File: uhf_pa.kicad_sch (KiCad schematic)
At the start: 24 parts, among them U12 FPF2701, U13 TQP7M9106

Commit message: Add manufacture number and JLCPCB part number to components
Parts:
- C67: JLCPCB Part # (none) -> C88885; Manufacturer_Part_Number (none) -> GJM1555C1H2R0WB01D
- C68: JLCPCB Part # (none) -> C2168987; Manufacturer_Part_Number (none) -> CGA2B3X5R1H104K050BB
- C70, C75, C76: JLCPCB Part # (none) -> C386123; Manufacturer_Part_Number (none) -> UMK105CG101JV-F
- C71: JLCPCB Part # (none) -> C2182156; Manufacturer_Part_Number (none) -> EMK212BB7106KG-T
- C72: JLCPCB Part # (none) -> C1711; Manufacturer_Part_Number (none) -> CL21B104KBCNNNC
- C73: JLCPCB Part # (none) -> C1959557; Manufacturer_Part_Number (none) -> T495C106K035ATE400
- C74: JLCPCB Part # (none) -> C2195556; Manufacturer_Part_Number (none) -> C0402C102K5GECAUTO7411
- C77: JLCPCB Part # (none) -> C3833393; Manufacturer_Part_Number (none) -> UMK105CG240JV-F
- C78: JLCPCB Part # (none) -> C88892; Manufacturer_Part_Number (none) -> GJM1555C1H3R3WB01D
- FB1: JLCPCB Part # (none) -> C85832; Manufacturer_Part_Number (none) -> BLM18KG331SN1D
- L14: JLCPCB Part # (none) -> C2043867; Manufacturer_Part_Number (none) -> LQW15AN4N0B8ZD
- L16: JLCPCB Part # (none) -> C2049784; Manufacturer_Part_Number (none) -> LQW15AN68NJ0ZD
- L17: JLCPCB Part # (none) -> C344018; Manufacturer_Part_Number (none) -> LQW15AN18NJ80D
- L18: JLCPCB Part # (none) -> C341788; Manufacturer_Part_Number (none) -> LQW15AN8N2H00D
- L19: JLCPCB Part # (none) -> C3222081; Manufacturer_Part_Number (none) -> LQW15AN47NJ8ZD
- R27: JLCPCB Part # (none) -> C843898; Manufacturer_Part_Number (none) -> CRCW0402240RFKEDC
- R28: JLCPCB Part # (none) -> C273692; Manufacturer_Part_Number (none) -> RC0402FR-07280RL
- R30, R31: JLCPCB Part # (none) -> C4176290; Manufacturer_Part_Number (none) -> ERJ-H3EF1103V
- U12: JLCPCB Part # (none) -> C891252; Manufacturer_Part_Number (none) -> FPF2701MPX
- U13: JLCPCB Part # (none) -> C920265; Manufacturer_Part_Number (none) -> TQP7M9106
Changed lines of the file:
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@@
+      (effects (font (size 1.27 1.27)) hide)
+    )
+    (property "JLCPCB Part #" "C344018" (id 5) (at 175.26 123.19 0)
+      (effects (font (size 1.27 1.27)) hide)
+    )
+    (property "Manufacturer_Part_Number" "LQW15AN18NJ80D " (id 6) (at 175.26 123.19 0)
       (effects (font (size 1.27 1.27)) hide)
     )
@@
     )
     (property "PartNumber" "LQW15AN47NJ8ZD" (id 4) (at 201.93 127 0)
+      (effects (font (size 1.27 1.27)) hide)
+    )
+    (property "JLCPCB Part #" "C3222081" (id 5) (at 201.93 127 0)
+      (effects (font (size 1.27 1.27)) hide)
+    )
+    (property "Manufacturer_Part_Number" "LQW15AN47NJ8ZD " (id 6) (at 201.93 127 0)
       (effects (font (size 1.27 1.27)) hide)
     )
@@
     )
     (property "PartNumber" "EMK212BB7106KG-T" (id 6) (at 144.78 33.02 0)
+      (effects (font (size 1.27 1.27)) hide)
+    )
+    (property "JLCPCB Part #" "C2182156" (id 7) (at 144.78 33.02 0)
+      (effects (font (size 1.27 1.27)) hide)
+    )
+    (property "Manufacturer_Part_Number" "EMK212BB7106KG-T" (id 8) (at 144.78 33.02 0)
       (effects (font (size 1.27 1.27)) hide)
     )
@@
       (effects (font (size 1.27 1.27)) hide)
     )
+    (property "JLCPCB Part #" "C2168987" (id 7) (at 100.33 106.68 0)
+      (effects (font (size 1.27 1.27)) hide)
+    )
+    (property "Manufacturer_Part_Number" "CGA2B3X5R1H104K050BB " (id 8) (at 100.33 106.68 0)
+      (effects (font (size 1.27 1.27)) hide)
+    )
     (pin "1")
     (pin "2")
@@
     )
     (property "PartNumber" "FPF2701MPX" (id 5) (at 139.7 49.53 0)
+      (effects (font (size 1.27 1.27)) hide)
+    )
+    (property "Manufacturer_Part_Number" "FPF2701MPX " (id 6) (at 139.7 49.53 0)
+      (effects (font (size 1.27 1.27)) hide)
+    )
+    (property "JLCPCB Part #" "C891252" (id 7) (at 139.7 49.53 0)
       (effects (font (size 1.27 1.27)) hide)
     )
@@
       (effects (font (size 1.27 1.27)) hide)
     )
+    (property "JLCPCB Part #" "C2049784" (id 7) (at 107.95 111.76 0)
+      (effects (font (size 1.27 1.27)) hide)
+    )
+    (property "Manufacturer_Part_Number" "LQW15AN68NJ0ZD " (id 8) (at 107.95 111.76 0)
+      (effects (font (size 1.27 1.27)) hide)
+    )
     (pin "1")
     (pin "2")
@@
       (effects (font (size 1.27 1.27)) hide)
     )
+    (property "JLCPCB Part #" "C2195556" (id 7) (at 180.34 101.6 0)
+      (effects (font (size 1.27 1.27)) hide)
+    )
+    (property "Manufacturer_Part_Number" "C0402C102K5GECAUTO7411 " (id 8) (at 180.34 101.6 0)
+      (effects (font (size 1.27 1.27)) hide)
+    )
     (pin "1")
     (pin "2")
@@
     )
     (property "PartNumber" "" (id 6) (at 115.57 96.52 0)
+      (effects (font (size 1.27 1.27)) hide)
+    )
+    (property "JLCPCB Part #" "C273692" (id 7) (at 115.57 96.52 0)
+      (effects (font (size 1.27 1.27)) hide)
+    )
+    (property "Manufacturer_Part_Number" "RC0402FR-07280RL " (id 8) (at 115.57 96.52 0)
       (effects (font (size 1.27 1.27)) hide)
     )
@@
       (effects (font (size 1.27 1.27)) hide)
     )
+    (property "JLCPCB Part #" "C3833393" (id 6) (at 189.23 127 0)
+      (effects (font (size 1.27 1.27)) hide)
+    )
+    (property "Manufacturer_Part_Number" "UMK105CG240JV-F" (id 7) (at 189.23 127 0)
+      (effects (font (size 1.27 1.27)) hide)
+    )
     (pin "1")
     (pin "2")
@@
       (effects (font (size 1.27 1.27)) hide)
     )
+    (property "JLCPCB Part #" "C386123" (id 7) (at 180.34 119.38 0)
+      (effects (font (size 1.27 1.27)) hide)
+    )
+    (property "Manufacturer_Part_Number" "UMK105CG101JV-F" (id 8) (at 180.34 119.38 0)
+      (effects (font (size 1.27 1.27)) hide)
+    )
     (pin "1")
     (pin "2")
@@
     )
     (property "PartNumber" "" (id 6) (at 107.95 96.52 0)
+      (effects (font (size 1.27 1.27)) hide)
+    )
+    (property "JLCPCB Part #" "C843898" (id 7) (at 107.95 96.52 0)
+      (effects (font (size 1.27 1.27)) hide)
+    )
+    (property "Manufacturer_Part_Number" "CRCW0402240RFKEDC " (id 8) (at 107.95 96.52 0)
       (effects (font (size 1.27 1.27)) hide)
     )
@@
     )
     (property "PartNumber" "" (id 6) (at 116.84 46.99 0)
+      (effects (font (size 1.27 1.27)) hide)
+    )
+    (property "JLCPCB Part #" "C4176290" (id 7) (at 116.84 46.99 0)
+      (effects (font (size 1.27 1.27)) hide)
+    )
+    (property "Manufacturer_Part_Number" "ERJ-H3EF1103V" (id 8) (at 116.84 46.99 0)
       (effects (font (size 1.27 1.27)) hide)
     )
@@
       (effects (font (size 1.27 1.27)) hide)
     )
+    (property "JLCPCB Part #" "C386123" (id 7) (at 180.34 110.49 0)
+      (effects (font (size 1.27 1.27)) hide)
+    )
+    (property "Manufacturer_Part_Number" "UMK105CG101JV-F" (id 8) (at 180.34 110.49 0)
+      (effects (font (size 1.27 1.27)) hide)
+    )
     (pin "1")
     (pin "2")
@@
       (effects (font (size 1.27 1.27)) hide)
     )
+    (property "JLCPCB Part #" "C1959557" (id 7) (at 180.34 92.71 0)
+      (effects (font (size 1.27 1.27)) hide)
+    )
+    (property "Manufacturer_Part_Number" "T495C106K035ATE400 " (id 8) (at 180.34 92.71 0)
+      (effects (font (size 1.27 1.27)) hide)
+    )
     (pin "1")
     (pin "2")
@@
       (effects (font (size 1.27 1.27)) hide)
     )
+    (property "JLCPCB Part #" "C4176290" (id 7) (at 127 59.69 0)
+      (effects (font (size 1.27 1.27)) hide)
+    )
+    (property "Manufacturer_Part_Number" "ERJ-H3EF1103V" (id 8) (at 127 59.69 0)
+      (effects (font (size 1.27 1.27)) hide)
+    )
     (pin "1")
     (pin "2")
@@
       (effects (font (size 1.27 1.27)) hide)
     )
+    (property "JLCPCB Part #" "C1711" (id 7) (at 160.02 33.02 0)
+      (effects (font (size 1.27 1.27)) hide)
+    )
+    (property "Manufacturer_Part_Number" "CL21B104KBCNNNC " (id 8) (at 160.02 33.02 0)
+      (effects (font (size 1.27 1.27)) hide)
+    )
     (pin "1")
     (pin "2")
@@
     )
     (property "PartNumber" "LQW15AN6N0B80D" (id 4) (at 119.38 133.35 0)
+      (effects (font (size 1.27 1.27)) hide)
+    )
+    (property "JLCPCB Part #" "C2043867" (id 5) (at 119.38 133.35 0)
+      (effects (font (size 1.27 1.27)) hide)
+    )
+    (property "Manufacturer_Part_Number" "LQW15AN4N0B8ZD " (id 6) (at 119.38 133.35 0)
       (effects (font (size 1.27 1.27)) hide)
     )
@@
       (effects (font (size 1.27 1.27)) hide)
     )
+    (property "JLCPCB Part #" "C88892" (id 6) (at 214.63 127 0)
+      (effects (font (size 1.27 1.27)) hide)
+    )
+    (property "Manufacturer_Part_Number" "GJM1555C1H3R3WB01D " (id 7) (at 214.63 127 0)
+      (effects (font (size 1.27 1.27)) hide)
+    )
     (pin "1")
     (pin "2")
@@
     )
     (property "PartNumber" "LQW15AN8N2H00D" (id 4) (at 195.58 132.08 0)
+      (effects (font (size 1.27 1.27)) hide)
+    )
+    (property "JLCPCB Part #" "C341788" (id 5) (at 195.58 132.08 0)
+      (effects (font (size 1.27 1.27)) hide)
+    )
+    (property "Manufacturer_Part_Number" "LQW15AN8N2H00D " (id 6) (at 195.58 132.08 0)
       (effects (font (size 1.27 1.27)) hide)
     )
@@
       (effects (font (size 1.27 1.27)) hide)
     )
+    (property "JLCPCB Part #" "C386123" (id 7) (at 121.92 106.68 0)
+      (effects (font (size 1.27 1.27)) hide)
+    )
+    (property "Manufacturer_Part_Number" "UMK105CG101JV-F" (id 8) (at 121.92 106.68 0)
+      (effects (font (size 1.27 1.27)) hide)
+    )
     (pin "1")
     (pin "2")
@@
       (effects (font (size 1.27 1.27)) (justify right) hide)
     )
+    (property "JLCPCB Part #" "C85832" (id 6) (at 175.26 114.3 0)
+      (effects (font (size 1.27 1.27)) hide)
+    )
+    (property "Manufacturer_Part_Number" "BLM18KG331SN1D " (id 7) (at 175.26 114.3 0)
+      (effects (font (size 1.27 1.27)) hide)
+    )
     (pin "1")
     (pin "2")
@@
     )
     (property "PartNumber" "GJM1555C1H2R0WB01D" (id 5) (at 127 128.27 0)
+      (effects (font (size 1.27 1.27)) hide)
+    )
+    (property "JLCPCB Part #" "C88885" (id 6) (at 127 128.27 0)
+      (effects (font (size 1.27 1.27)) hide)
+    )
+    (property "Manufacturer_Part_Number" "GJM1555C1H2R0WB01D " (id 7) (at 127 128.27 0)
       (effects (font (size 1.27 1.27)) hide)
     )
@@
       (effects (font (size 1.27 1.27)) hide)
     )
+    (property "Manufacturer_Part_Number" "TQP7M9106 " (id 6) (at 151.13 127 0)
+      (effects (font (size 1.27 1.27)) hide)
+    )
+    (property "JLCPCB Part #" "C920265" (id 7) (at 151.13 127 0)
+      (effects (font (size 1.27 1.27)) hide)
+    )

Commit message: Update C67 part number
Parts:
- C67: JLCPCB Part # C88885 -> C576707; Manufacturer_Part_Number GJM1555C1H2R0WB01D -> CC0402JRNPO9BN500; Mnf. Murata Electronics -> (none); PartNumber GJM1555C1H2R0WB01D -> CC0402JRNPO9BN500
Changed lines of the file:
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@@
       (effects (font (size 1.27 1.27)) hide)
     )
-    (property "Mnf." "Murata Electronics" (id 4) (at 127 128.27 0)
+    (property "PartNumber" "CC0402JRNPO9BN500 " (id 5) (at 127 128.27 0)
       (effects (font (size 1.27 1.27)) hide)
     )
-    (property "PartNumber" "GJM1555C1H2R0WB01D" (id 5) (at 127 128.27 0)
+    (property "JLCPCB Part #" "C576707" (id 6) (at 127 128.27 0)
       (effects (font (size 1.27 1.27)) hide)
     )
-    (property "JLCPCB Part #" "C88885" (id 6) (at 127 128.27 0)
+    (property "Manufacturer_Part_Number" "CC0402JRNPO9BN500 " (id 7) (at 127 128.27 0)
       (effects (font (size 1.27 1.27)) hide)
     )
-    (property "Manufacturer_Part_Number" "GJM1555C1H2R0WB01D " (id 7) (at 127 128.27 0)
-      (effects (font (size 1.27 1.27)) hide)
-    )

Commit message: Update the manufacturer part number for some of components to be compatible with avaiable parts in the JLC parts database
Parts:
- C72: JLCPCB Part # C1711 -> C141125; Manufacturer_Part_Number CL21B104KBCNNNC -> C0805C104K1RACAUTO
- C74: JLCPCB Part # C2195556 -> C129636; Manufacturer_Part_Number C0402C102K5GECAUTO7411 -> C0805C102J5RACAUTO
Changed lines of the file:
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@@
       (effects (font (size 1.27 1.27)) hide)
     )
-    (property "JLCPCB Part #" "C2195556" (id 7) (at 180.34 101.6 0)
-      (effects (font (size 1.27 1.27)) hide)
-    )
-    (property "Manufacturer_Part_Number" "C0402C102K5GECAUTO7411 " (id 8) (at 180.34 101.6 0)
+    (property "JLCPCB Part #" "C129636" (id 7) (at 180.34 101.6 0)
+      (effects (font (size 1.27 1.27)) hide)
+    )
+    (property "Manufacturer_Part_Number" "C0805C102J5RACAUTO" (id 8) (at 180.34 101.6 0)
       (effects (font (size 1.27 1.27)) hide)
     )
@@
       (effects (font (size 1.27 1.27)) hide)
     )
-    (property "JLCPCB Part #" "C1711" (id 7) (at 160.02 33.02 0)
-      (effects (font (size 1.27 1.27)) hide)
-    )
-    (property "Manufacturer_Part_Number" "CL21B104KBCNNNC " (id 8) (at 160.02 33.02 0)
-      (effects (font (size 1.27 1.27)) hide)
-    )
+    (property "JLCPCB Part #" "C141125" (id 7) (at 160.02 33.02 0)
+      (effects (font (size 1.27 1.27)) hide)
+    )
+    (property "Manufacturer_Part_Number" "C0805C104K1RACAUTO" (id 8) (at 160.02 33.02 0)
+      (effects (font (size 1.27 1.27)) hide)
+    )

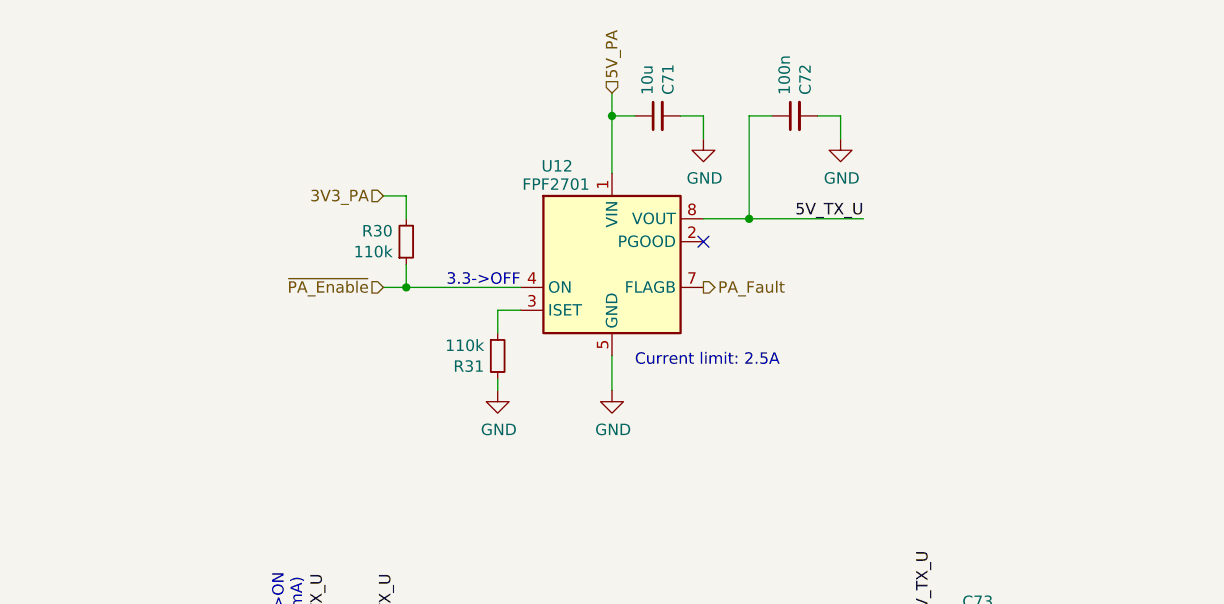
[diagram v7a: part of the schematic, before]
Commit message: Replace the U12 from FPF2702 to TPS22950-Q1: R30 is pulling down, R31: 110K -> 470 Ohm, U7 is removed, since ON is active high now
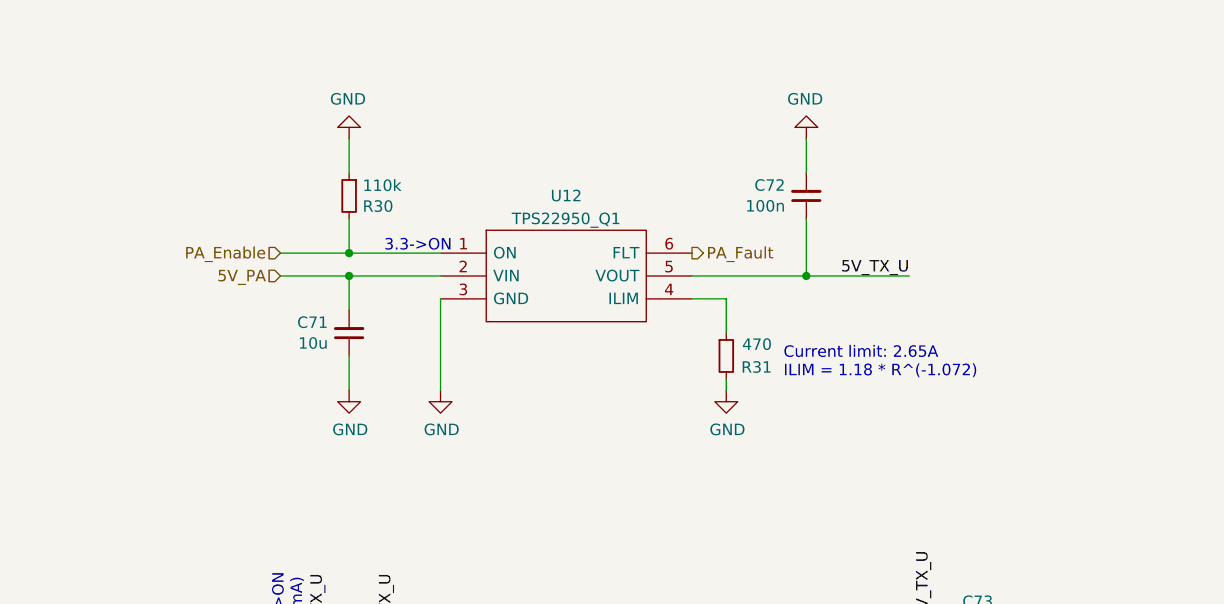
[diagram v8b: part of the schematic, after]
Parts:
- R31: value 110k -> 470
- U12: value FPF2701 -> TPS22950_Q1; footprint lsf-kicad-lib:MLP-8 -> Package_TO_SOT_SMD:TSOT-23-6; symbol lsf-kicad-lib:FPF2701 -> STS1_COBC_V2-rescue:TPS22950CQDDCRQ1; Height (none) -> 1.1; JLCPCB Part # C891252 -> C17349276; Manufacturer_Name (none) -> Texas Instruments; Manufacturer_Part_Number FPF2701MPX -> TPS22950CQDDCRQ1; Mnf. ON Semiconductor / Fairchild -> Texas Instrument; Mouser Part Number (none) -> 595-TPS22950CQDDCRQ1; Mouser Price/Stock (none) -> https://www.mouser.co.uk/ProductDetail/Texas-Instruments/TP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; PartNumber FPF2701MPX -> TPS22950CQDDCRQ1
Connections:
- net 5V_PA: now also C71.2, U12.2 (VIN); no longer C71.1, U12.1 (VIN)
- net 5V_TX_U: now also U12.5 (VOUT); no longer U12.8 (VOUT)
- net GND: now also C71.1, R30.1, U12.3 (GND); no longer C71.2, U12.5 (GND), U12.9 (GND)
- net PA_Fault: now also U12.6 (FLT); no longer U12.7 (FLAGB)
- net at R31.1: now also U12.4 (ILIM); no longer U12.3 (ISET)
- net 3V3_PA renamed PA_Enable
- net PA_Enable: now also U12.1 (ON)
- removed net ~{PA_Enable}: R30.1, U12.4 (ON)
- no-connect marks 1 -> 0
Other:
- note added: "3.3->ON"
- note added: "Current limit: 2.65A ILIM = 1.18 * R^(-1.072)"
- note removed: "3.3->OFF"
- note removed: "Current limit: 2.5A"
- moved on the sheet: C71, C72, R30, R31
